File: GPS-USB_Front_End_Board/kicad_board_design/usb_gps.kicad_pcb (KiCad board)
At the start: 4 copper layers, 99.1 x 53.3 mm, 228 parts, among them J1 Micro-USB Connector, J3 SMA, P1 CONN_02X12, P2 CONN_01X03, U1 93LCxxB, U2 FT2232HL-REEL, U3 L4931 LDO, U4 MAX8510, U5 MAX8510, U6 MAX2771, U7 SAWTEK-855969, U8 LT1719S6 -- Not Populated, X1 13.368MHz TCXO, Y1 12MHz Crystal

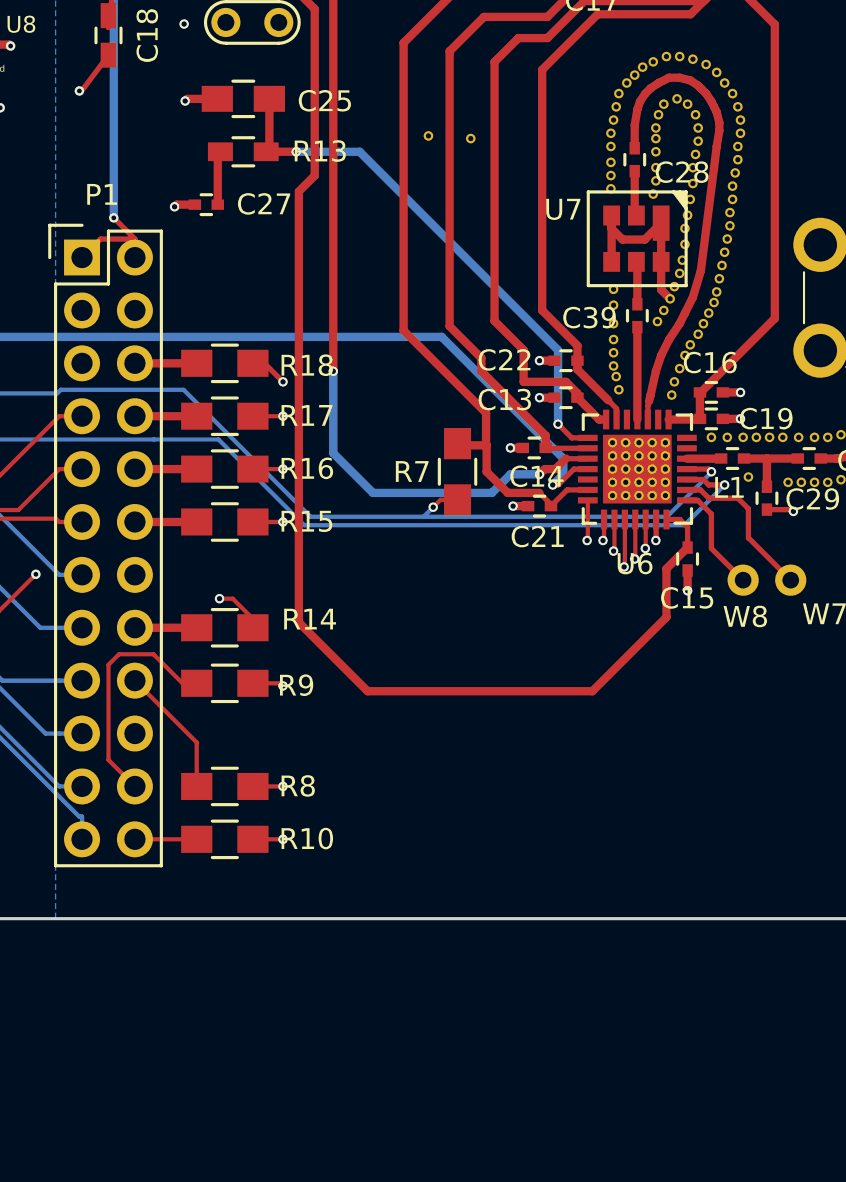
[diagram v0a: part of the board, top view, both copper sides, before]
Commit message: Run DRC, generate and import netlist w/ new caps.
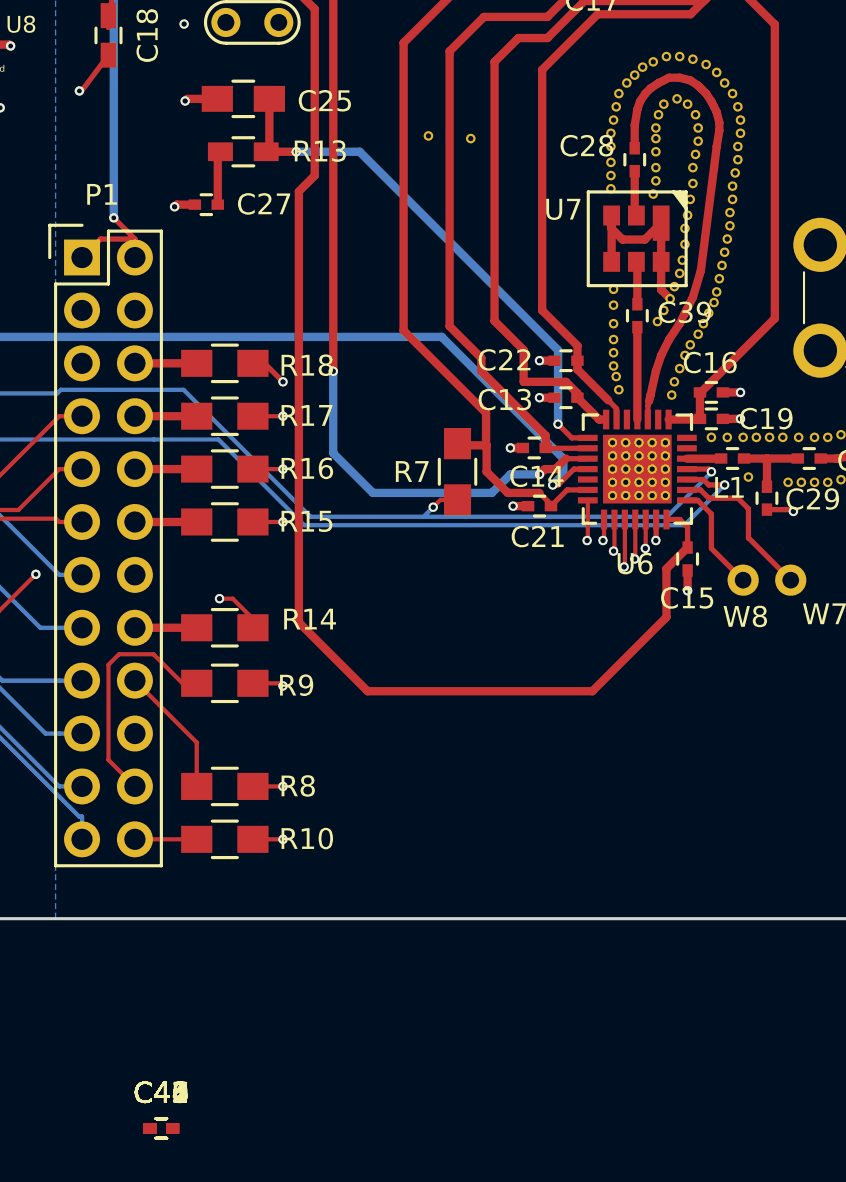
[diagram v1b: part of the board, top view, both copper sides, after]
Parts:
- added C40, C41, C44, C45, C46, C47, C48: .1uF, Capacitors_SMD:C_0402, F.Cu at (132.1, 124.4)
- added C42, C43: 4.7uF, Capacitors_SMD:C_0402, F.Cu at (132.1, 124.4)
- C19: value .1nF -> 100pF
- C23, C36, C7: value 2.2uF -> 10uF
- C28, C39: value .47nF -> 470pF
- C33, C35, C9: value 100 nF -> .1uF
- C37: value 100nF -> .1uF
- turned C28 to 90 degrees
- turned C39 to 90 degrees
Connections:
- C39 pad 1: /MAX_2769/MIXIN -> Net-(C39-Pad1)
- C39 pad 2: Net-(C39-Pad2) -> /MAX_2769/MIXIN
- U6 pad 24: Net-(C28-Pad1) -> Net-(C28-Pad2)
- U6 pad 25: Net-(C39-Pad2) -> Net-(C39-Pad1)
- U7 pad 2: Net-(C28-Pad2) -> Net-(C28-Pad1)
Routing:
- net Net-(C28-Pad1): track 22.5 -> 2.16 mm
- net Net-(C28-Pad2): track 2.16 -> 22.5 mm
- net Net-(C39-Pad2): track 4.44 -> 0.00 mm
- net Net-(C39-Pad1): track 0.00 -> 4.44 mm

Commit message: Partially laid out; ready to move some parts.
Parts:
- C34, C4: footprint Capacitors_SMD:C_0805_HandSoldering -> Capacitors_SMD:C_0402
- C7: footprint Capacitors_SMD:C_0805_HandSoldering -> Capacitors_SMD:C_0805
- moved C40 46.9 mm to (101.9, 88.5), turned to 90 degrees
- moved C45 44.9 mm to (106.8, 87.3), turned to 90 degrees
- moved C46 44.2 mm to (98.9, 95.1), turned to 180 degrees
- moved C47 43.3 mm to (109.7, 87.3), turned to 90 degrees
- moved C48 41.8 mm to (111.2, 88.2), turned to 90 degrees
- moved C42 35.2 mm to (104.5, 102.5), turned to 270 degrees
- moved C44 35.2 mm to (114.1, 94.1)
- moved C41 33.0 mm to (114.1, 96.6)
- moved W2 32.8 mm to (115.3, 79.2)
- moved C5 31.8 mm to (90.4, 86.1), turned to 90 degrees
- moved C43 31.0 mm to (110.1, 102.5), turned to 270 degrees
- moved W3 30.4 mm to (115.3, 82.3)
- moved TP6 29.2 mm to (87.9, 87.4)
- moved R6 28.7 mm to (109.7, 79.2)
- moved R5 27.4 mm to (108.7, 75.2), turned to 270 degrees
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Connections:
- C48 pad 1: /MAX_2769/VCC3V3 -> /USB_FT2232/VREGOUT
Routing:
- net /USB_FT2232/RESET: track 37.4 -> 0.00 mm, vias 1 -> 0
- net GND: track 125.6 -> 90.7 mm, vias 43 -> 60
- net /USB_FT2232/SCS: track 33.7 -> 1.23 mm, vias 1 -> 0
- net /MAX_2769/+5V: track 116.8 -> 148.4 mm, vias 3 -> 2
- net Net-(C26-Pad1): track 42.6 -> 11.7 mm, vias 2 -> 1
- net Net-(C3-Pad1): track 43.0 -> 12.9 mm, vias 2 -> 0
- net /USB_FT2232/SCLK: track 30.0 -> 1.09 mm, vias 1 -> 0
- net /USB_FT2232/GPIO1: track 58.9 -> 31.8 mm, vias 2 -> 1
- net /USB_FT2232/GPIO0: track 61.2 -> 38.1 mm, vias 3 -> 2
- net /USB_FT2232/REF: track 22.3 -> 0.00 mm, vias 2 -> 0
- net /USB_FT2232/EECLK: track 42.6 -> 21.6 mm, vias 1 -> 0
- net /USB_FT2232/OSCO: track 33.9 -> 16.0 mm, vias 1 -> 0
- net /USB_FT2232/WR#: track 17.0 -> 0.00 mm, vias 1 -> 0
- net Net-(R6-Pad1): track 43.5 -> 27.4 mm, vias 1 -> 0
- net /USB_FT2232/EECS: track 35.0 -> 19.6 mm
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
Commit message: Now passes DRC.
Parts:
- moved C37 35.0 mm to (120.0, 103.6), turned to 180 degrees
- moved C38 30.5 mm to (118.6, 98.2)
- moved U8 29.9 mm to (119.8, 101.1), turned to 180 degrees
- moved R20 29.5 mm to (122.7, 101.1), turned to 90 degrees
- moved TP5 28.3 mm to (92.3, 63.0)
- moved X1 27.3 mm to (142.2, 92.1), turned to 270 degrees
- moved C20 27.0 mm to (147.7, 93.3), turned to 0 degrees
- moved C26 25.0 mm to (137.1, 97.8)
- moved R19 23.3 mm to (123.1, 97.8), turned to 0 degrees
- moved C11 22.8 mm to (144.6, 90.0), turned to 0 degrees
- moved R7 7.59 mm to (150.6, 99.1)
- moved W5 6.49 mm to (115.4, 103.8)
- moved W2 1.91 mm to (117.2, 79.2)
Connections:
- C26 pad 2: Net-(C26-Pad2) -> /MAX_2769/CLKOUT
- R19 pad 1: /MAX_2769/CLKOUT -> /USB_FT2232/WR_fix#
- R19 pad 2: Net-(C26-Pad2) -> /USB_FT2232/WR#
- R20 pad 2: Net-(C26-Pad2) -> /USB_FT2232/WR#
- U2 pad 54: /USB_FT2232/WR# -> /USB_FT2232/WR_fix#
- U8 pad 3: Net-(C26-Pad2) -> /USB_FT2232/WR#
- U8 pad 5: /MAX_2769/CLKOUT -> /USB_FT2232/WR_fix#
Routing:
- net /USB_FT2232/GPIO1: track 31.8 -> 75.6 mm, vias 1 -> 2
- net /USB_FT2232/GPIO0: track 38.1 -> 76.7 mm, vias 2 -> 3
- net Net-(C20-Pad2): track 38.7 -> 4.37 mm, vias 2 -> 0
- net /USB_FT2232/SCS: track 1.23 -> 35.1 mm, vias 0 -> 1
- net /USB_FT2232/WR_fix#: track 0.00 -> 30.8 mm, vias 0 -> 2
- net /MAX_2769/VCCA: track 188.5 -> 218.7 mm
- net /USB_FT2232/SCLK: track 1.09 -> 30.3 mm, vias 0 -> 1
- net /USB_FT2232/TXE#: track 1.09 -> 28.1 mm, vias 0 -> 1
- net /MAX_2769/CLKOUT: track 23.3 -> 2.93 mm, vias 1 -> 0
- net /USB_FT2232/REF: track 0.00 -> 14.3 mm, vias 0 -> 2
- net /USB_FT2232/WR#: track 0.00 -> 9.72 mm
- net /MAX_2769/VCC3V3: track 92.9 -> 102.6 mm, vias 16 -> 18
- net /USB_FT2232/RESET: track 0.00 -> 9.10 mm
- net /USB_FT2232/EECLK: track 21.6 -> 29.9 mm
- net Net-(C26-Pad1): track 11.7 -> 18.4 mm, vias 1 -> 2
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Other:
- board text added: "rev. 3, 11/01/2019"
- board text removed: "rev. 2, 7/28/2019"

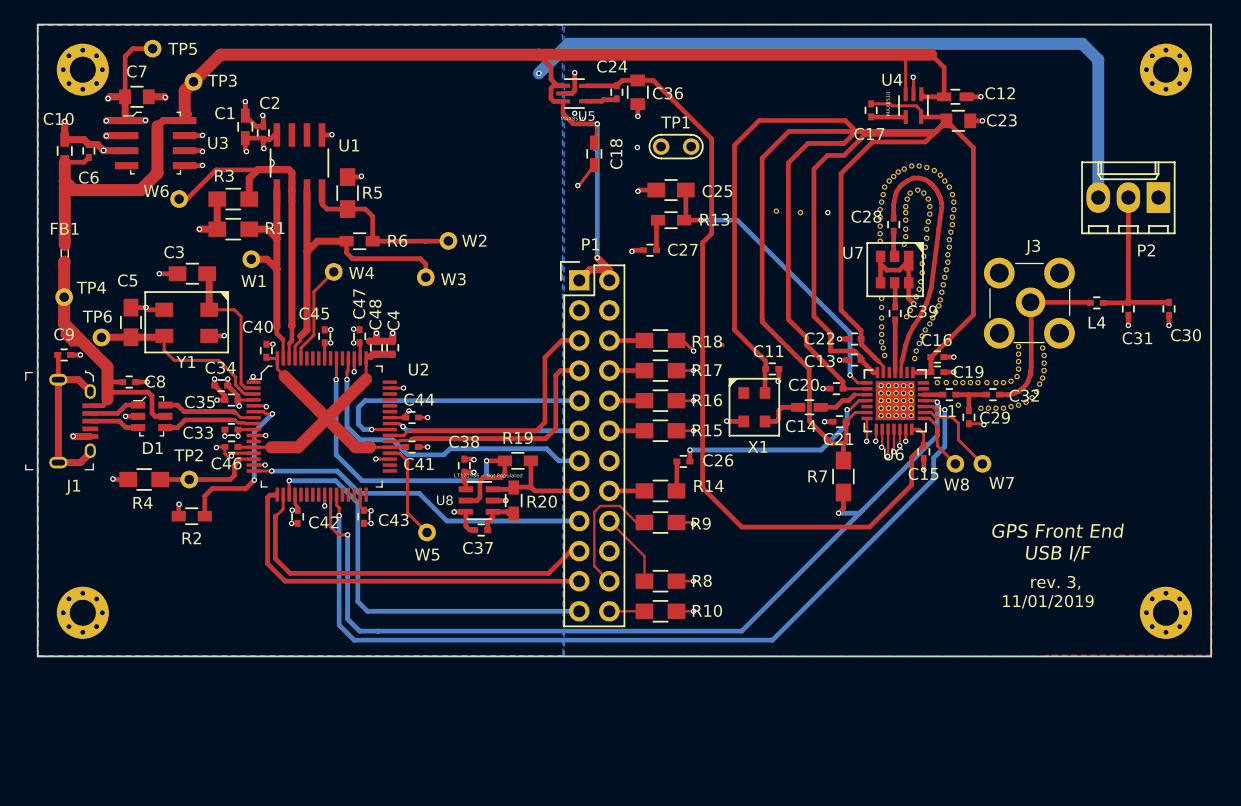
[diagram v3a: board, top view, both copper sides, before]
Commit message: Plotted gerbers.  Fixed crystal load caps, added LED, added stitching.
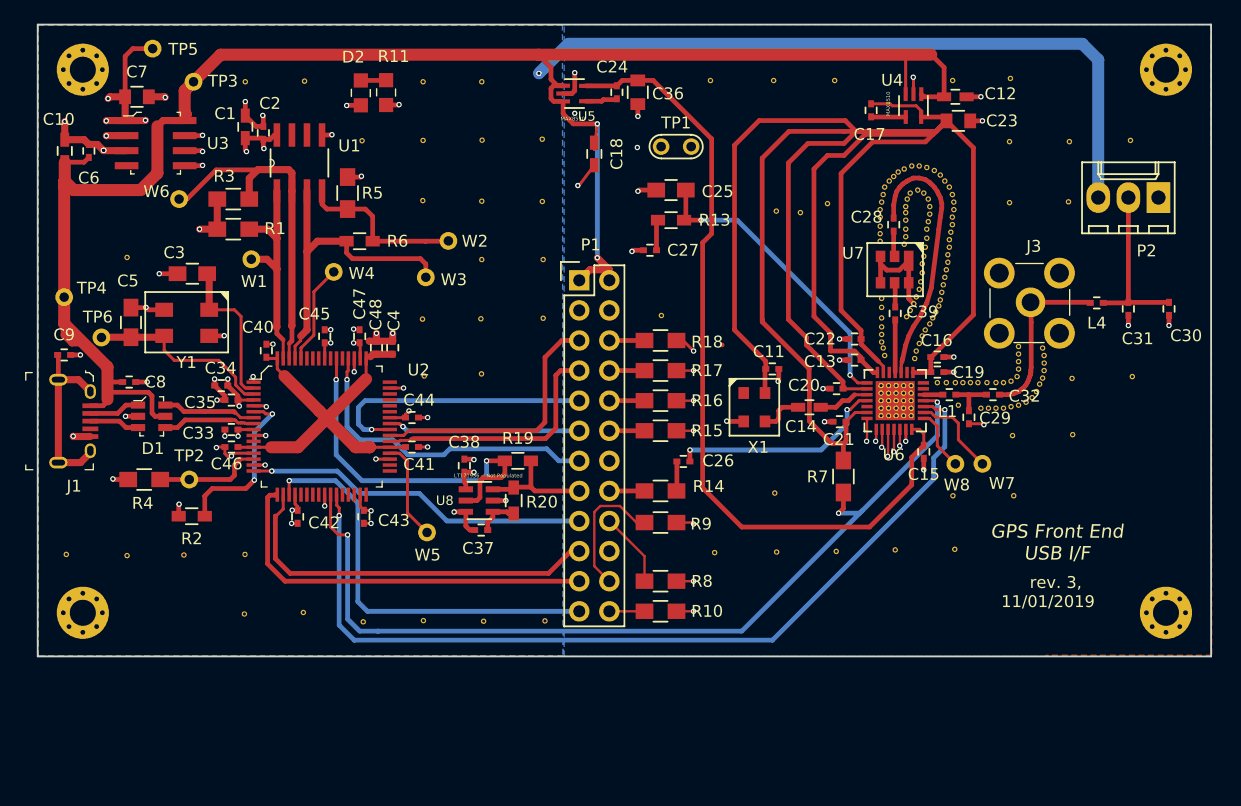
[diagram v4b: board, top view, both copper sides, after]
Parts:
- removed FB1: BLM18PG471SN1D, digikey-footprints:0603
- added D2: LTST-C171KRKT, digikey-footprints:0805, F.Cu at (109.8, 66.7)
- added R11: 200, digikey-footprints:0805, F.Cu at (112.0, 66.7)
- added REF**: via_10mil, logo:via_10mil, F.Cu at (174.8, 70.7)
- added REF**: via_10mil, logo:via_10mil, F.Cu at (139.3, 65.7)
- added REF**: via_10mil, logo:via_10mil, F.Cu at (144.8, 100.5)
- added REF**: via_10mil, logo:via_10mil, F.Cu at (175.0, 90.7)
- added REF**: via_10mil, logo:via_10mil, F.Cu at (169.9, 90.8)
- added REF**: via_10mil, logo:via_10mil, F.Cu at (169.9, 95.6)
- added REF**: via_10mil, logo:via_10mil, F.Cu at (164.8, 95.7)
- added REF**: via_10mil, logo:via_10mil, F.Cu at (164.9, 100.7)
- added REF**: via_10mil, logo:via_10mil, F.Cu at (159.8, 100.7)
- added REF**: via_10mil, logo:via_10mil, F.Cu at (160.0, 105.3)
- added REF**: via_10mil, logo:via_10mil, F.Cu at (154.9, 105.3)
- added REF**: via_10mil, logo:via_10mil, F.Cu at (169.6, 70.8)
- added REF**: via_10mil, logo:via_10mil, F.Cu at (150.0, 105.4)
- added REF**: via_10mil, logo:via_10mil, F.Cu at (144.9, 105.5)
- added REF**: via_10mil, logo:via_10mil, F.Cu at (139.7, 105.5)
- added REF**: via_10mil, logo:via_10mil, F.Cu at (125.4, 111.3)
- added REF**: via_10mil, logo:via_10mil, F.Cu at (120.2, 111.3)
- added REF**: via_10mil, logo:via_10mil, F.Cu at (115.1, 111.3)
- added REF**: via_10mil, logo:via_10mil, F.Cu at (110.0, 111.4)
- added REF**: via_10mil, logo:via_10mil, F.Cu at (105.0, 110.6)
- added REF**: via_10mil, logo:via_10mil, F.Cu at (100.0, 110.7)
- added REF**: via_10mil, logo:via_10mil, F.Cu at (100.1, 105.7)
- added REF**: via_10mil, logo:via_10mil, F.Cu at (169.6, 75.9)
- added REF**: via_10mil, logo:via_10mil, F.Cu at (85.0, 105.7)
- added REF**: via_10mil, logo:via_10mil, F.Cu at (94.9, 105.7)
- added REF**: via_10mil, logo:via_10mil, F.Cu at (90.1, 105.8)
- added REF**: via_10mil, logo:via_10mil, F.Cu at (120.0, 90.4)
- added REF**: via_10mil, logo:via_10mil, F.Cu at (115.2, 90.6)
- added REF**: via_10mil, logo:via_10mil, F.Cu at (90.1, 80.6)
- added REF**: via_10mil, logo:via_10mil, F.Cu at (135.2, 85.5)
- added REF**: via_10mil, logo:via_10mil, F.Cu at (125.2, 85.8)
- added REF**: via_10mil, logo:via_10mil, F.Cu at (115.0, 85.8)
- added REF**: via_10mil, logo:via_10mil, F.Cu at (120.0, 85.8)
- added REF**: via_10mil, logo:via_10mil, F.Cu at (164.6, 76.0)
- added REF**: via_10mil, logo:via_10mil, F.Cu at (125.2, 80.8)
- added REF**: via_10mil, logo:via_10mil, F.Cu at (120.0, 80.8)
- added REF**: via_10mil, logo:via_10mil, F.Cu at (125.1, 75.9)
- added REF**: via_10mil, logo:via_10mil, F.Cu at (120.0, 75.9)
- added REF**: via_10mil, logo:via_10mil, F.Cu at (115.1, 75.8)
- added REF**: via_10mil, logo:via_10mil, F.Cu at (125.1, 70.6)
- added REF**: via_10mil, logo:via_10mil, F.Cu at (120.1, 70.7)
- added REF**: via_10mil, logo:via_10mil, F.Cu at (115.1, 70.7)
- added REF**: via_10mil, logo:via_10mil, F.Cu at (109.9, 70.8)
- added REF**: via_10mil, logo:via_10mil, F.Cu at (120.0, 65.8)
- added REF**: via_10mil, logo:via_10mil, F.Cu at (164.6, 70.8)
- added REF**: via_10mil, logo:via_10mil, F.Cu at (115.1, 65.8)
- added REF**: via_10mil, logo:via_10mil, F.Cu at (105.1, 65.7)
- added REF**: via_10mil, logo:via_10mil, F.Cu at (100.1, 65.8)
- added REF**: via_10mil, logo:via_10mil, F.Cu at (149.2, 76.1)
- added REF**: via_10mil, logo:via_10mil, F.Cu at (164.7, 65.5)
- added REF**: via_10mil, logo:via_10mil, F.Cu at (159.8, 65.7)
- added REF**: via_10mil, logo:via_10mil, F.Cu at (149.8, 65.7)
- added REF**: via_10mil, logo:via_10mil, F.Cu at (144.7, 65.7)
- C3, C5: value 10pF -> 33pF
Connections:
- C8 pad 1: /USB_FT2232/VBUS -> /MAX_2769/+5V
- D1 pad 5: /USB_FT2232/VBUS -> /MAX_2769/+5V
- J1 pad 1: /USB_FT2232/VBUS -> /MAX_2769/+5V
- TP4 pad 1: /USB_FT2232/VBUS -> /MAX_2769/+5V
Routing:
- net /MAX_2769/+5V: track 152.8 -> 187.2 mm
- net /USB_FT2232/VBUS: track 32.4 -> 0.00 mm
- net (no net): track 3.74 -> 1.25 mm, vias 3 -> 2
- net Net-(D2-Pad2): track 0.00 -> 2.14 mm
- net GND: track 97.1 -> 98.3 mm, vias 64 -> 65
- net /MAX_2769/VCC3V3: track 102.6 -> 103.7 mm, vias 18 -> 19
